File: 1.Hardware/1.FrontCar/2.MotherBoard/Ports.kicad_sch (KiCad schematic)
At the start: 2 parts

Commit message: update .gitignore
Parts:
- added H?: (no value), symbol ErBW_s:Maple
- added J?: PWR, Connector:VCC_CONN, symbol Connector_Generic:Conn_01x02
- J?: value MOTOR -> (none); footprint Connector:VCC_CONN -> (none)
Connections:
- net GNDPWR: now also J?.2 (Pin_2)
- net VBUS: now also J?.1 (Pin_1)
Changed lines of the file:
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@@
+    (stroke (width 0) (type default) (color 0 0 0 0))
+  )
+  (wire (pts (xy 110.49 43.18) (xy 111.76 43.18))
     (stroke (width 0) (type default) (color 0 0 0 0))
   )
@@
     (stroke (width 0) (type default) (color 0 0 0 0))
   )
+  (wire (pts (xy 110.49 40.64) (xy 111.76 40.64))
+    (stroke (width 0) (type default) (color 0 0 0 0))
+  )
   (text "Copyright (c) 2022, ErBW_s\nAll rights reserved." (at 186.69 180.34 0)
     (effects (font (size 4.318 4.318)) (justify left bottom))
   )
+  (symbol (lib_id "power:GNDPWR") (at 110.49 43.18 0) (unit 1)
+    (in_bom yes) (on_board yes) (fields_autoplaced)
+    (property "Reference" "#PWR?" (id 0) (at 110.49 48.26 0)
+      (effects (font (size 1.27 1.27)) hide)
+    )
+    (property "Value" "GNDPWR" (id 1) (at 110.363 47.217 0))
+    (property "Footprint" "" (id 2) (at 110.49 44.45 0)
+      (effects (font (size 1.27 1.27)) hide)
+    )
+    (property "Datasheet" "" (id 3) (at 110.49 44.45 0)
+      (effects (font (size 1.27 1.27)) hide)
+    )
+    (pin "1")
+  )
+  (symbol (lib_id "Connector_Generic:Conn_01x02") (at 116.84 40.64 0) (unit 1)
+    (in_bom yes) (on_board yes)
+    (property "Reference" "J?" (id 0) (at 118.872 41.0753 0)
+      (effects (font (size 1.27 1.27)) (justify left))
+    )
+    (property "Value" "" (id 1) (at 118.872 43.6122 0)
+      (effects (font (size 1.27 1.27)) (justify left))
+    )
+    (property "Footprint" "" (id 2) (at 116.84 40.64 0)
+      (effects (font (size 1.27 1.27)) hide)
+    )
+    (property "Datasheet" "" (id 3) (at 116.84 40.64 0)
+      (effects (font (size 1.27 1.27)) hide)
+    )
+    (property "Datasheet" "" (id 4) (at 116.84 40.64 0)
+      (effects (font (size 1.27 1.27)) hide)
+    )
+    (property "Footprint" "Connector:VCC_CONN" (id 5) (at 116.84 40.64 0)
+      (effects (font (size 1.27 1.27)) hide)
+    )
+    (property "Reference" "J?" (id 6) (at 116.84 40.64 0)
+      (effects (font (size 1.27 1.27)) hide)
+    )
+    (property "Value" "PWR" (id 7) (at 116.84 40.64 0)
+      (effects (font (size 1.27 1.27)) hide)
+    )
+    (pin "1")
+    (pin "2")
+  )
   (symbol (lib_id "power:VBUS") (at 110.49 57.15 0) (unit 1)
     (in_bom yes) (on_board yes) (fields_autoplaced)
-    (property "Reference" "#PWR?" (id 0) (at 110.49 60.96 0)
+    (property "Reference" "#PWR0120" (id 0) (at 110.49 60.96 0)
       (effects (font (size 1.27 1.27)) hide)
     )
@@
     (pin "1")
   )
+  (symbol (lib_id "ErBW_s:Maple") (at 173.355 68.58 0) (unit 1)
+    (in_bom yes) (on_board yes) (fields_autoplaced)
+    (property "Reference" "H?" (id 0) (at 173.355 59.8002 0))
+    (property "Value" "" (id 1) (at 173.355 62.3371 0))
+    (property "Footprint" "" (id 2) (at 173.355 77.47 0)
+      (effects (font (size 1.27 1.27)) hide)
+    )
+    (property "Datasheet" "" (id 3) (at 170.815 66.04 0)
+      (effects (font (size 1.27 1.27)) hide)
+    )
+    (pin "1")
+    (pin "2")
+    (pin "3")
+    (pin "4")
+    (pin "5")
+    (pin "6")
+  )
   (symbol (lib_id "Connector_Generic:Conn_01x02") (at 116.84 57.15 0) (unit 1)
     (in_bom yes) (on_board yes)
@@
       (effects (font (size 1.27 1.27)) (justify left))
     )
-    (property "Value" "PWR" (id 1) (at 118.872 60.1222 0)
+    (property "Value" "" (id 1) (at 118.872 60.1222 0)
       (effects (font (size 1.27 1.27)) (justify left))
     )
-    (property "Footprint" "Connector:VCC_CONN" (id 2) (at 116.84 57.15 0)
+    (property "Footprint" "" (id 2) (at 116.84 57.15 0)
       (effects (font (size 1.27 1.27)) hide)
     )
@@
   (symbol (lib_id "power:VCC") (at 110.49 73.66 0) (unit 1)
     (in_bom yes) (on_board yes) (fields_autoplaced)
-    (property "Reference" "#PWR?" (id 0) (at 110.49 77.47 0)
+    (property "Reference" "#PWR0122" (id 0) (at 110.49 77.47 0)
       (effects (font (size 1.27 1.27)) hide)
     )
@@
       (effects (font (size 1.27 1.27)) (justify left))
     )
-    (property "Value" "MOTOR" (id 1) (at 118.872 76.6322 0)
+    (property "Value" "" (id 1) (at 118.872 76.6322 0)
       (effects (font (size 1.27 1.27)) (justify left))
     )
-    (property "Footprint" "Connector:VCC_CONN" (id 2) (at 116.84 73.66 0)
+    (property "Footprint" "" (id 2) (at 116.84 73.66 0)
       (effects (font (size 1.27 1.27)) hide)
     )
@@
     (pin "2")
   )
+  (symbol (lib_id "power:VBUS") (at 110.49 40.64 0) (unit 1)
+    (in_bom yes) (on_board yes) (fields_autoplaced)
+    (property "Reference" "#PWR?" (id 0) (at 110.49 44.45 0)
+      (effects (font (size 1.27 1.27)) hide)
+    )
+    (property "Value" "VBUS" (id 1) (at 110.49 37.0642 0))
+    (property "Footprint" "" (id 2) (at 110.49 40.64 0)
+      (effects (font (size 1.27 1.27)) hide)
+    )
+    (property "Datasheet" "" (id 3) (at 110.49 40.64 0)
+      (effects (font (size 1.27 1.27)) hide)
+    )
+    (pin "1")
+  )
   (symbol (lib_id "power:GNDPWR") (at 110.49 76.2 0) (unit 1)
     (in_bom yes) (on_board yes) (fields_autoplaced)
-    (property "Reference" "#PWR?" (id 0) (at 110.49 81.28 0)
+    (property "Reference" "#PWR0123" (id 0) (at 110.49 81.28 0)
       (effects (font (size 1.27 1.27)) hide)
     )
@@
   (symbol (lib_id "power:GNDPWR") (at 110.49 59.69 0) (unit 1)
     (in_bom yes) (on_board yes) (fields_autoplaced)
-    (property "Reference" "#PWR?" (id 0) (at 110.49 64.77 0)
+    (property "Reference" "#PWR0121" (id 0) (at 110.49 64.77 0)
       (effects (font (size 1.27 1.27)) hide)
     )

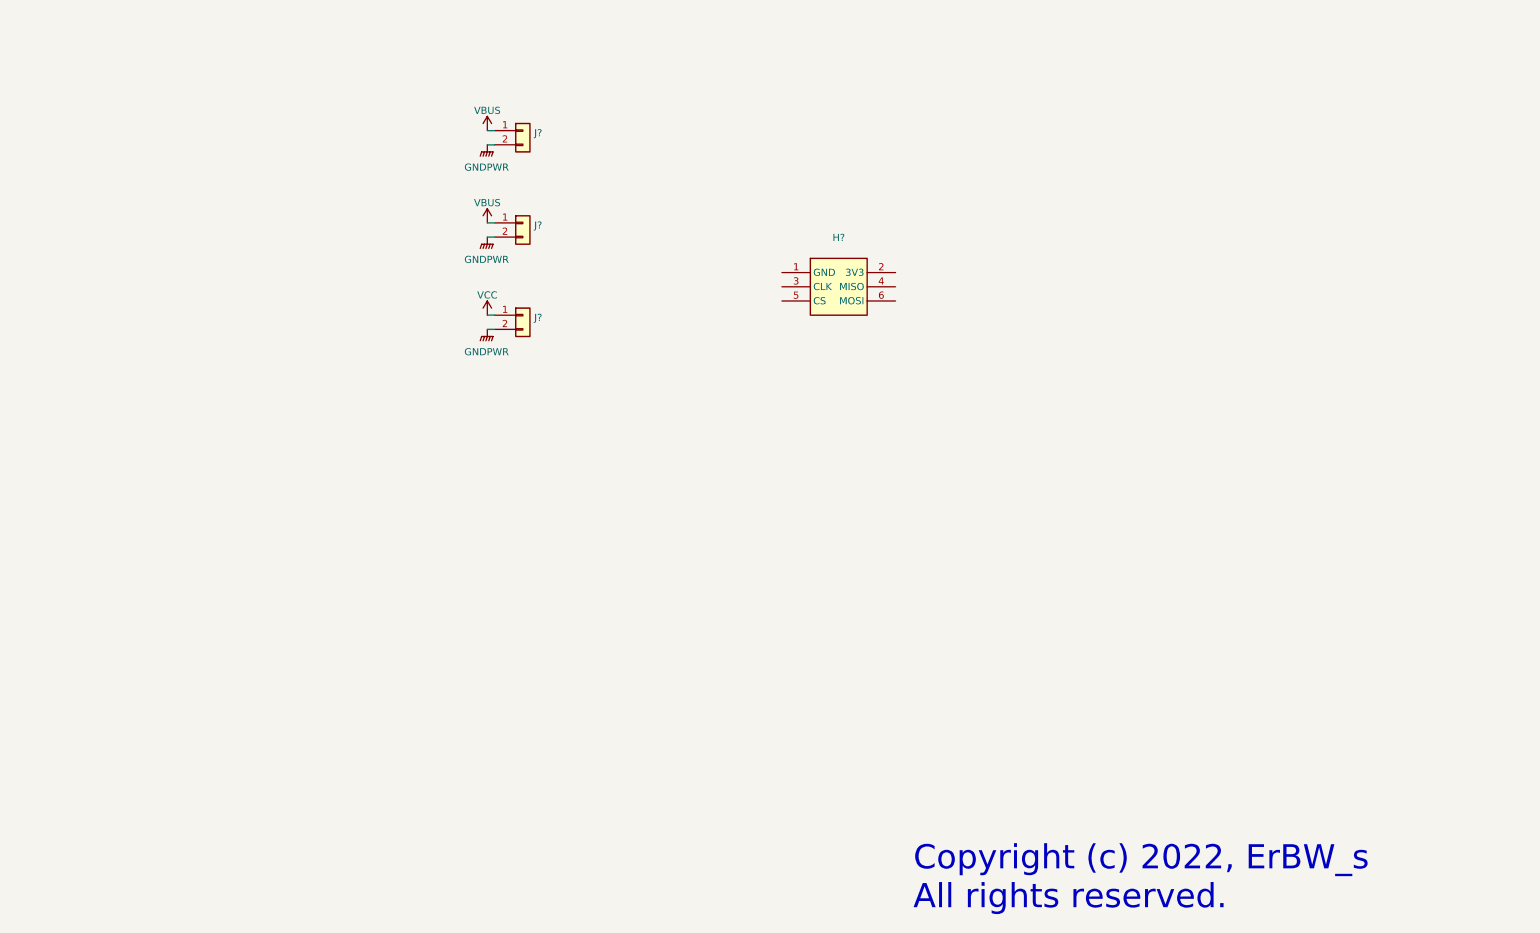
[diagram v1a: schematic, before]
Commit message: 母板原理图完成
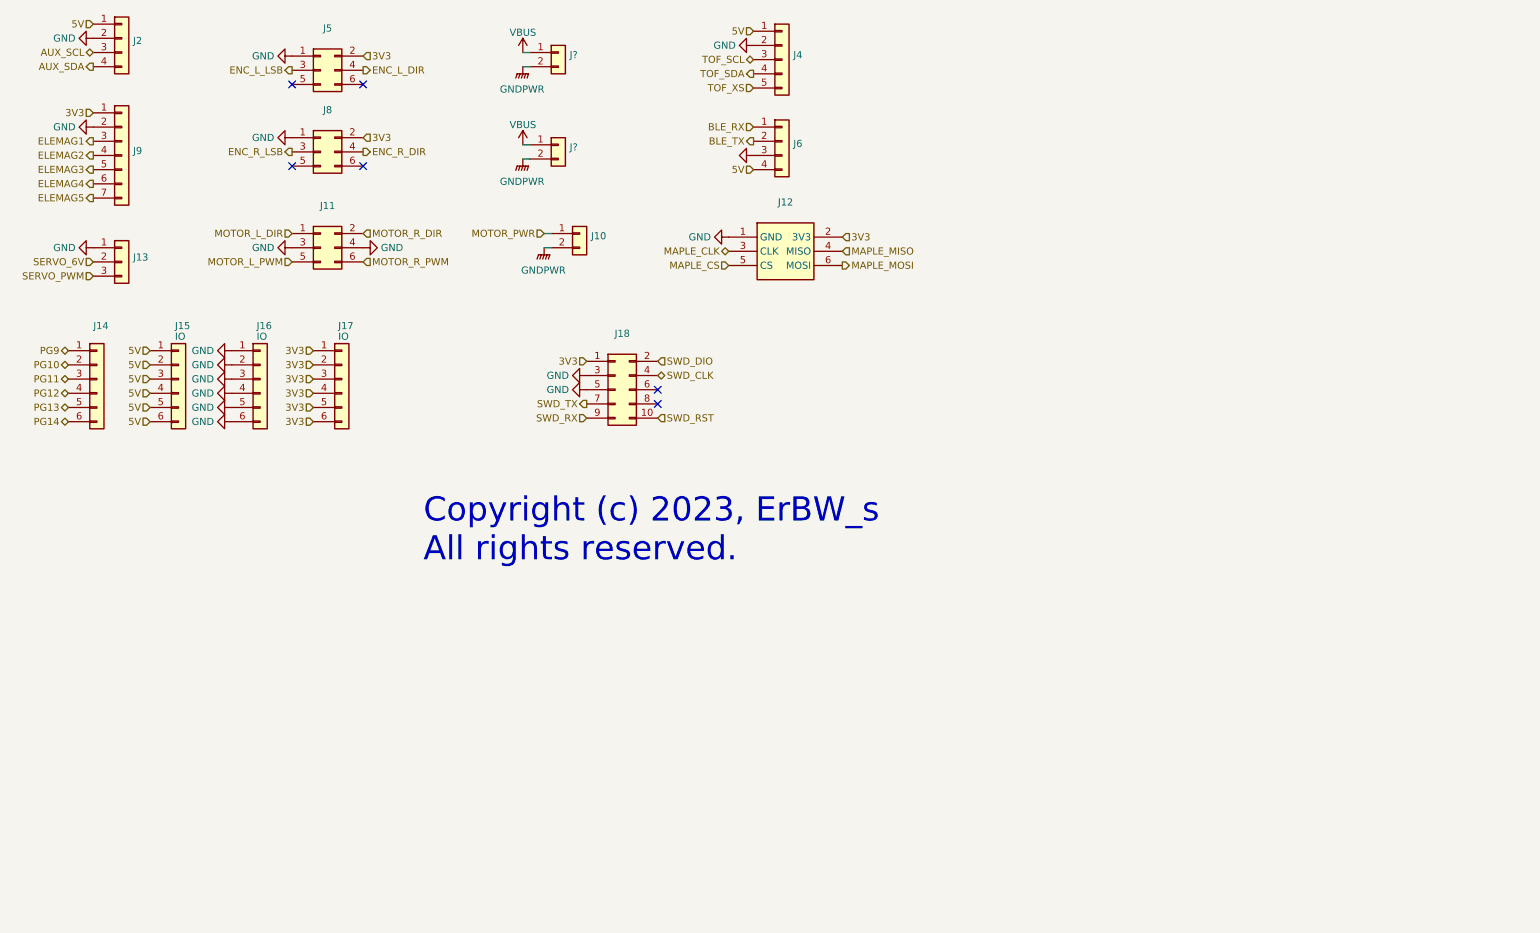
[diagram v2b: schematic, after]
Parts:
- added J11, J5: (no value), symbol Connector_Generic:Conn_02x03_Odd_Even
- added J13: (no value), symbol Connector_Generic:Conn_01x03
- added J14: (no value), symbol Connector_Generic:Conn_01x06
- added J15, J16, J17: IO, symbol Connector_Generic:Conn_01x06
- added J18: (no value), symbol Connector_Generic:Conn_02x05_Odd_Even
- added J2, J6: (no value), symbol Connector_Generic:Conn_01x04
- added J4: (no value), symbol Connector_Generic:Conn_01x05
- added J8: (no value), Connector_PinHeader_2.54mm:PinHeader_2x03_P2.54mm_Vertical, symbol Connector_Generic:Conn_02x03_Odd_Even
- added J9: (no value), symbol Connector_Generic:Conn_01x07
- gave numbers to parts that had none: 2
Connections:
- net GND: now reaches J12.1 (GND)
- net GND: now also J11.3 (Pin_3), J11.4 (Pin_4), J13.1 (Pin_1), J16.1 (Pin_1), J16.2 (Pin_2), J16.3 (Pin_3), J16.4 (Pin_4), J16.5 (Pin_5), J16.6 (Pin_6), J18.3 (Pin_3), J18.5 (Pin_5), J2.2 (Pin_2), J4.2 (Pin_2), J5.1 (Pin_1), J6.3 (Pin_3), J8.1 (Pin_1), J9.2 (Pin_2)
- net 3V3: now reaches J12.2 (3V3)
- net 3V3: now also J17.1 (Pin_1), J17.2 (Pin_2), J17.3 (Pin_3), J17.4 (Pin_4), J17.5 (Pin_5), J17.6 (Pin_6), J18.1 (Pin_1), J5.2 (Pin_2), J8.2 (Pin_2), J9.1 (Pin_1)
- net MAPLE_CLK: now reaches J12.3 (CLK)
- net MAPLE_MISO: now reaches J12.4 (MISO)
- net MAPLE_CS: now reaches J12.5 (CS)
- net MAPLE_MOSI: now reaches J12.6 (MOSI)
- net VCC renamed MOTOR_PWR
- new net 5V: J15.1 (Pin_1), J15.2 (Pin_2), J15.3 (Pin_3), J15.4 (Pin_4), J15.5 (Pin_5), J15.6 (Pin_6), J2.1 (Pin_1), J4.1 (Pin_1), J6.4 (Pin_4)
- new net AUX_SCL: J2.3 (Pin_3)
- new net AUX_SDA: J2.4 (Pin_4)
- new net BLE_RX: J6.1 (Pin_1)
- new net BLE_TX: J6.2 (Pin_2)
- new net ELEMAG1: J9.3 (Pin_3)
- new net ELEMAG2: J9.4 (Pin_4)
- new net ELEMAG3: J9.5 (Pin_5)
- new net ELEMAG4: J9.6 (Pin_6)
- new net ELEMAG5: J9.7 (Pin_7)
- new net ENC_L_DIR: J5.4 (Pin_4)
- new net ENC_L_LSB: J5.3 (Pin_3)
- new net ENC_R_DIR: J8.4 (Pin_4)
- new net ENC_R_LSB: J8.3 (Pin_3)
- new net MOTOR_L_DIR: J11.1 (Pin_1)
- new net MOTOR_L_PWM: J11.5 (Pin_5)
- new net MOTOR_R_DIR: J11.2 (Pin_2)
- new net MOTOR_R_PWM: J11.6 (Pin_6)
- new net PG10: J14.2 (Pin_2)
- new net PG11: J14.3 (Pin_3)
- new net PG12: J14.4 (Pin_4)
- new net PG13: J14.5 (Pin_5)
- new net PG14: J14.6 (Pin_6)
- new net PG9: J14.1 (Pin_1)
- new net SERVO_6V: J13.2 (Pin_2)
- new net SERVO_PWM: J13.3 (Pin_3)
- new net SWD_CLK: J18.4 (Pin_4)
- new net SWD_DIO: J18.2 (Pin_2)
- new net SWD_RST: J18.10 (Pin_10)
- new net SWD_RX: J18.9 (Pin_9)
- new net SWD_TX: J18.7 (Pin_7)
- new net TOF_SCL: J4.3 (Pin_3)
- new net TOF_SDA: J4.4 (Pin_4)
- new net TOF_XS: J4.5 (Pin_5)
- no-connect marks 0 -> 6
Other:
- note added: "Copyright (c) 2023, ErBW_s All rights reserved."
- note removed: "Copyright (c) 2022, ErBW_s All rights reserved."
- moved on the sheet: J10, J12, J?

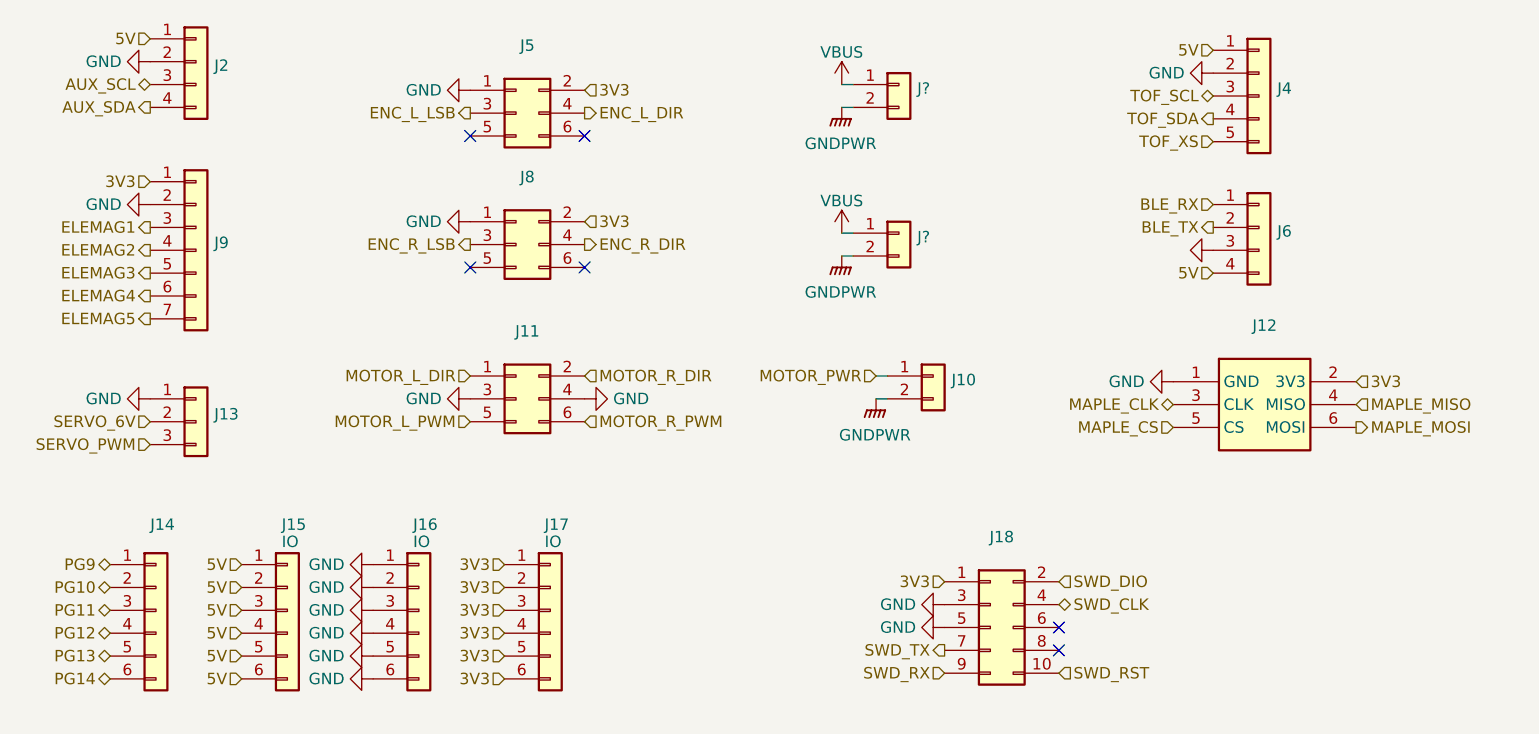
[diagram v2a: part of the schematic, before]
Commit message: 更新母板原理图封装
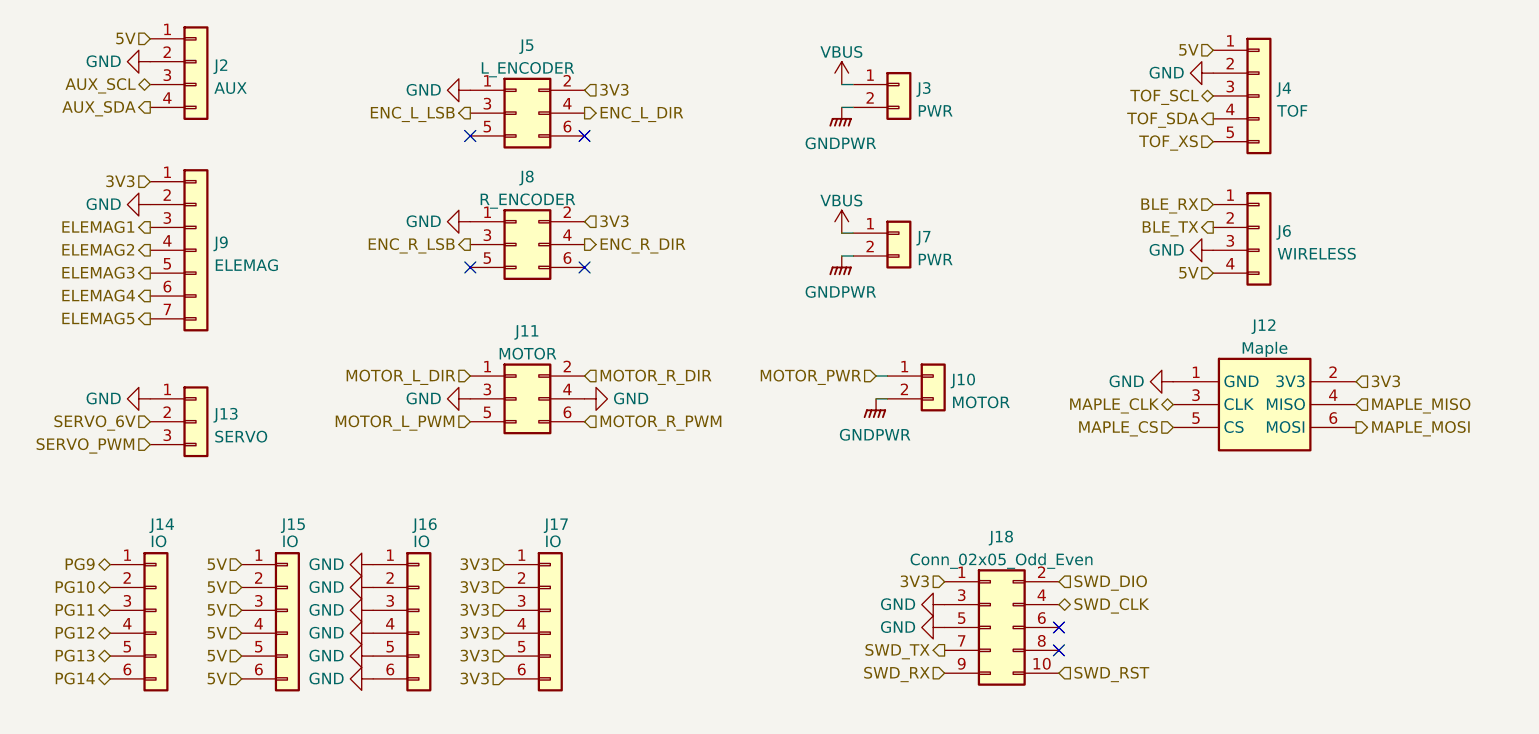
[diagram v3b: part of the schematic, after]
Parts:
- J10: value (none) -> MOTOR; footprint (none) -> Connector_AMASS:AMASS_XT30U-M_1x02_P5.0mm_Vertical
- J11: value (none) -> MOTOR; footprint (none) -> Connector_PinHeader_2.54mm:PinHeader_2x03_P2.54mm_Vertical
- J12: value (none) -> Maple; footprint (none) -> ErBW_s:Maple
- J13: value (none) -> SERVO; footprint (none) -> Connector_PinHeader_2.54mm:PinHeader_1x03_P2.54mm_Vertical
- J14: value (none) -> IO; footprint (none) -> Connector_PinHeader_2.54mm:PinHeader_1x06_P2.54mm_Vertical
- J15, J16, J17: footprint (none) -> Connector_PinHeader_2.54mm:PinHeader_1x06_P2.54mm_Vertical
- J18: value (none) -> Conn_02x05_Odd_Even; footprint (none) -> Connector_PinHeader_2.54mm:PinHeader_2x05_P2.54mm_Vertical
- J2: value (none) -> AUX; footprint (none) -> Connector_PinHeader_2.54mm:PinHeader_1x04_P2.54mm_Vertical
- J4: value (none) -> TOF; footprint (none) -> Connector_PinHeader_2.54mm:PinHeader_1x05_P2.54mm_Vertical
- J5: value (none) -> L_ENCODER; footprint (none) -> Connector_PinHeader_2.54mm:PinHeader_2x03_P2.54mm_Vertical
- J6: value (none) -> WIRELESS; footprint (none) -> Connector_PinHeader_2.54mm:PinHeader_1x04_P2.54mm_Vertical
- J8: value (none) -> R_ENCODER
- J9: value (none) -> ELEMAG; footprint (none) -> Connector_PinHeader_2.54mm:PinHeader_1x07_P2.54mm_Vertical
- gave numbers to parts that had none: 2
